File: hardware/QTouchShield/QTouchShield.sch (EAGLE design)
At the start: 114 parts, among them IC1 AT32UC3C0512CJEDEC-MS-026, U1 ARDUINO-MEGALITE

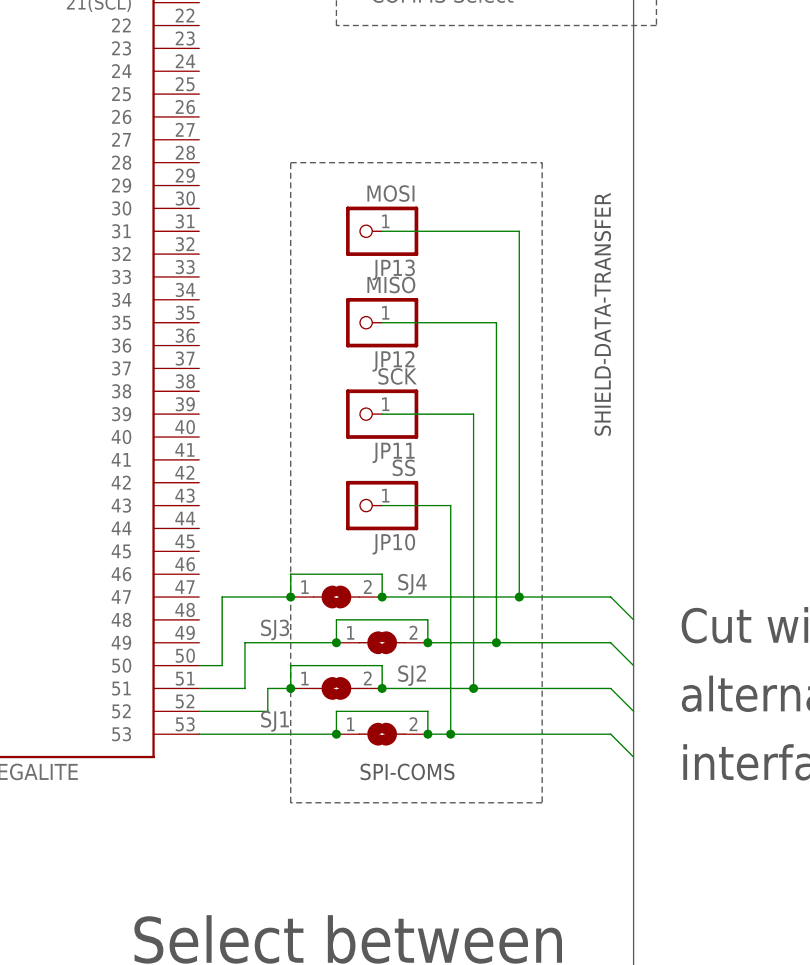
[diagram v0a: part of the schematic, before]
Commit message: Swapped MISO/MOSI connection to Arduino - wrong way round.
The MISO/MOSI lines from the UC3C to the Arduino were swapped.
Fixed in the schematic and board.
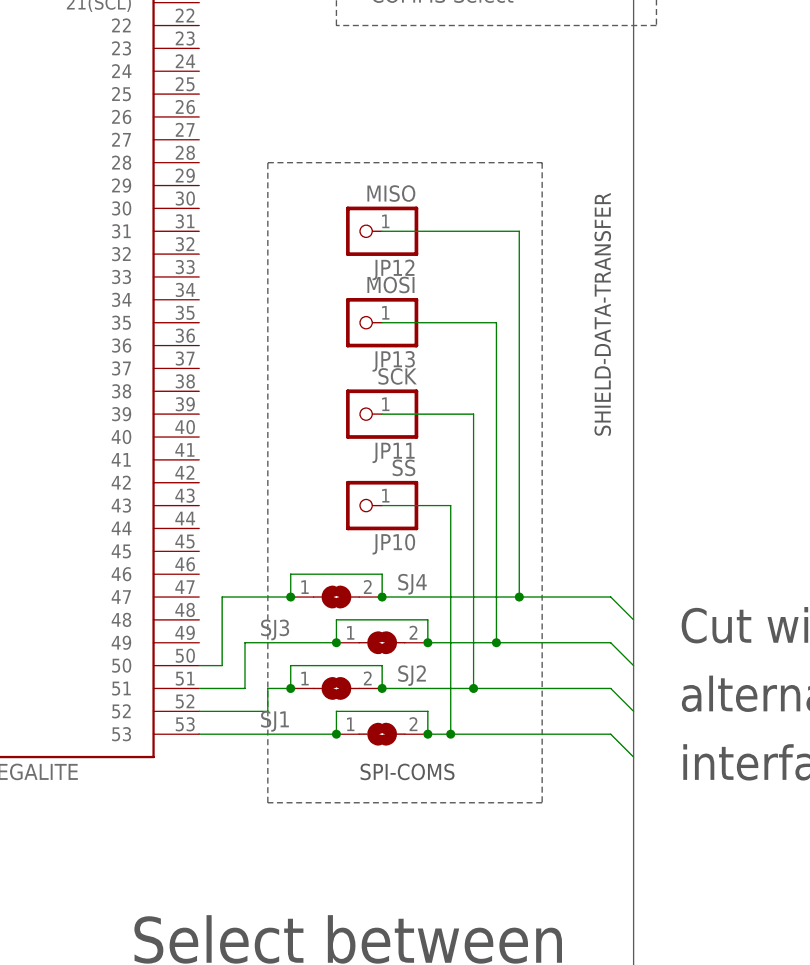
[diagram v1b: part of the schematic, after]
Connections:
- net SDT-SPI0-MISO: now also SJ4.1, SJ4.2, U1.50; no longer SJ3.1, SJ3.2, U1.51
- net SDT-SPI0-MOSI: now also SJ3.1, SJ3.2, U1.51; no longer SJ4.1, SJ4.2, U1.50
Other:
- moved on the sheet: JP12, JP13
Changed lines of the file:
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@@
 <setting verticaltext="up"/>
 </settings>
-<grid distance="0.1" unitdist="mm" unit="mm" style="lines" multiple="1" display="yes" altdistance="0.01" altunitdist="inch" altunit="inch"/>
+<grid distance="0.1" unitdist="inch" unit="inch" style="lines" multiple="1" display="no" altdistance="0.01" altunitdist="inch" altunit="inch"/>
 <layers>
 <layer number="1" name="Top" color="4" fill="1" visible="no" active="no"/>
@@
 <layer number="91" name="Nets" color="2" fill="1" visible="yes" active="yes"/>
 <layer number="92" name="Busses" color="1" fill="1" visible="yes" active="yes"/>
-<layer number="93" name="Pins" color="2" fill="1" visible="yes" active="yes"/>
+<layer number="93" name="Pins" color="2" fill="1" visible="no" active="yes"/>
 <layer number="94" name="Symbols" color="4" fill="1" visible="yes" active="yes"/>
 <layer number="95" name="Names" color="7" fill="1" visible="yes" active="yes"/>
@@
 <wire x1="-2.54" y1="-109.22" x2="-96.52" y2="-109.22" width="0.1524" layer="97" style="shortdash"/>
 <wire x1="-96.52" y1="-109.22" x2="-96.52" y2="-106.68" width="0.1524" layer="97" style="shortdash"/>
-<wire x1="256.54" y1="-45.72" x2="256.54" y2="25.4" width="0.1524" layer="97" style="shortdash"/>
-<wire x1="256.54" y1="25.4" x2="284.48" y2="25.4" width="0.1524" layer="97" style="shortdash"/>
+<wire x1="254" y1="-45.72" x2="254" y2="25.4" width="0.1524" layer="97" style="shortdash"/>
+<wire x1="254" y1="25.4" x2="284.48" y2="25.4" width="0.1524" layer="97" style="shortdash"/>
 <wire x1="284.48" y1="25.4" x2="284.48" y2="-45.72" width="0.1524" layer="97" style="shortdash"/>
-<wire x1="284.48" y1="-45.72" x2="256.54" y2="-45.72" width="0.1524" layer="97" style="shortdash"/>
+<wire x1="284.48" y1="-45.72" x2="254" y2="-45.72" width="0.1524" layer="97" style="shortdash"/>
 <text x="170.18" y="25.4" size="1.778" layer="97" rot="R90">Use to link AT32UC3C</text>
 <text x="172.72" y="25.4" size="1.778" layer="97" rot="R90">RESET_N to</text>
@@
 <instance part="JP10" gate="G$1" x="264.16" y="-12.7" rot="R180"/>
 <instance part="JP11" gate="G$1" x="264.16" y="-2.54" rot="R180"/>
-<instance part="JP12" gate="G$1" x="264.16" y="7.62" rot="R180"/>
-<instance part="JP13" gate="G$1" x="264.16" y="17.78" rot="R180"/>
+<instance part="JP12" gate="G$1" x="264.16" y="17.78" rot="R180"/>
+<instance part="JP13" gate="G$1" x="264.16" y="7.62" rot="R180"/>
 <instance part="JP14" gate="G$1" x="228.6" y="73.66" rot="R180"/>
 <instance part="JP15" gate="G$1" x="185.42" y="-7.62" rot="R180"/>
@@
 </segment>
 <segment>
-<wire x1="294.64" y1="-25.4" x2="292.1" y2="-22.86" width="0.1524" layer="91"/>
-<wire x1="292.1" y1="-22.86" x2="281.94" y2="-22.86" width="0.1524" layer="91"/>
-<pinref part="SJ4" gate="1" pin="2"/>
+<wire x1="294.64" y1="-30.48" x2="292.1" y2="-27.94" width="0.1524" layer="91"/>
+<pinref part="SJ3" gate="1" pin="2"/>
+<wire x1="279.4" y1="-27.94" x2="271.78" y2="-27.94" width="0.1524" layer="91"/>
+<pinref part="SJ3" gate="1" pin="1"/>
+<wire x1="261.62" y1="-27.94" x2="261.62" y2="-25.4" width="0.1524" layer="91"/>
+<wire x1="261.62" y1="-25.4" x2="271.78" y2="-25.4" width="0.1524" layer="91"/>
+<wire x1="271.78" y1="-25.4" x2="271.78" y2="-27.94" width="0.1524" layer="91"/>
+<junction x="271.78" y="-27.94"/>
+<wire x1="292.1" y1="-27.94" x2="279.4" y2="-27.94" width="0.1524" layer="91"/>
+<pinref part="U1" gate="G$1" pin="51"/>
+<wire x1="251.46" y1="-27.94" x2="251.46" y2="-33.02" width="0.1524" layer="91"/>
+<wire x1="251.46" y1="-33.02" x2="246.38" y2="-33.02" width="0.1524" layer="91"/>
+<wire x1="261.62" y1="-27.94" x2="251.46" y2="-27.94" width="0.1524" layer="91"/>
+<junction x="261.62" y="-27.94"/>
 <pinref part="JP13" gate="G$1" pin="1"/>
-<wire x1="281.94" y1="-22.86" x2="266.7" y2="-22.86" width="0.1524" layer="91"/>
-<wire x1="281.94" y1="-22.86" x2="281.94" y2="17.78" width="0.1524" layer="91"/>
-<wire x1="281.94" y1="17.78" x2="266.7" y2="17.78" width="0.1524" layer="91"/>
-<junction x="281.94" y="-22.86"/>
-<wire x1="256.54" y1="-22.86" x2="248.92" y2="-22.86" width="0.1524" layer="91"/>
-<wire x1="248.92" y1="-22.86" x2="248.92" y2="-30.48" width="0.1524" layer="91"/>
-<pinref part="U1" gate="G$1" pin="50"/>
-<wire x1="248.92" y1="-30.48" x2="246.38" y2="-30.48" width="0.1524" layer="91"/>
-<pinref part="SJ4" gate="1" pin="1"/>
-<wire x1="256.54" y1="-22.86" x2="256.54" y2="-20.32" width="0.1524" layer="91"/>
-<junction x="256.54" y="-22.86"/>
-<wire x1="256.54" y1="-20.32" x2="266.7" y2="-20.32" width="0.1524" layer="91"/>
-<wire x1="266.7" y1="-20.32" x2="266.7" y2="-22.86" width="0.1524" layer="91"/>
-<junction x="266.7" y="-22.86"/>
+<wire x1="266.7" y1="7.62" x2="279.4" y2="7.62" width="0.1524" layer="91"/>
+<wire x1="279.4" y1="7.62" x2="279.4" y2="-27.94" width="0.1524" layer="91"/>
+<junction x="279.4" y="-27.94"/>
 </segment>
 </net>
@@
 </segment>
 <segment>
-<wire x1="294.64" y1="-30.48" x2="292.1" y2="-27.94" width="0.1524" layer="91"/>
-<wire x1="292.1" y1="-27.94" x2="279.4" y2="-27.94" width="0.1524" layer="91"/>
-<pinref part="SJ3" gate="1" pin="2"/>
-<wire x1="279.4" y1="-27.94" x2="271.78" y2="-27.94" width="0.1524" layer="91"/>
-<wire x1="279.4" y1="-27.94" x2="279.4" y2="7.62" width="0.1524" layer="91"/>
-<wire x1="279.4" y1="7.62" x2="266.7" y2="7.62" width="0.1524" layer="91"/>
-<junction x="279.4" y="-27.94"/>
+<wire x1="294.64" y1="-25.4" x2="292.1" y2="-22.86" width="0.1524" layer="91"/>
+<pinref part="SJ4" gate="1" pin="2"/>
+<wire x1="281.94" y1="-22.86" x2="266.7" y2="-22.86" width="0.1524" layer="91"/>
+<pinref part="SJ4" gate="1" pin="1"/>
+<wire x1="256.54" y1="-22.86" x2="256.54" y2="-20.32" width="0.1524" layer="91"/>
+<wire x1="256.54" y1="-20.32" x2="266.7" y2="-20.32" width="0.1524" layer="91"/>
+<wire x1="266.7" y1="-20.32" x2="266.7" y2="-22.86" width="0.1524" layer="91"/>
+<junction x="266.7" y="-22.86"/>
+<wire x1="292.1" y1="-22.86" x2="281.94" y2="-22.86" width="0.1524" layer="91"/>
+<pinref part="U1" gate="G$1" pin="50"/>
+<wire x1="248.92" y1="-22.86" x2="248.92" y2="-30.48" width="0.1524" layer="91"/>
+<wire x1="248.92" y1="-30.48" x2="246.38" y2="-30.48" width="0.1524" layer="91"/>
+<wire x1="256.54" y1="-22.86" x2="248.92" y2="-22.86" width="0.1524" layer="91"/>
+<junction x="256.54" y="-22.86"/>
 <pinref part="JP12" gate="G$1" pin="1"/>
-<wire x1="261.62" y1="-27.94" x2="251.46" y2="-27.94" width="0.1524" layer="91"/>
-<wire x1="251.46" y1="-27.94" x2="251.46" y2="-33.02" width="0.1524" layer="91"/>
-<pinref part="U1" gate="G$1" pin="51"/>
-<wire x1="251.46" y1="-33.02" x2="246.38" y2="-33.02" width="0.1524" layer="91"/>
-<pinref part="SJ3" gate="1" pin="1"/>
-<wire x1="261.62" y1="-27.94" x2="261.62" y2="-25.4" width="0.1524" layer="91"/>
-<junction x="261.62" y="-27.94"/>
-<wire x1="261.62" y1="-25.4" x2="271.78" y2="-25.4" width="0.1524" layer="91"/>
-<wire x1="271.78" y1="-25.4" x2="271.78" y2="-27.94" width="0.1524" layer="91"/>
-<junction x="271.78" y="-27.94"/>
+<wire x1="266.7" y1="17.78" x2="281.94" y2="17.78" width="0.1524" layer="91"/>
+<wire x1="281.94" y1="17.78" x2="281.94" y2="-22.86" width="0.1524" layer="91"/>
+<junction x="281.94" y="-22.86"/>
 </segment>
 </net>

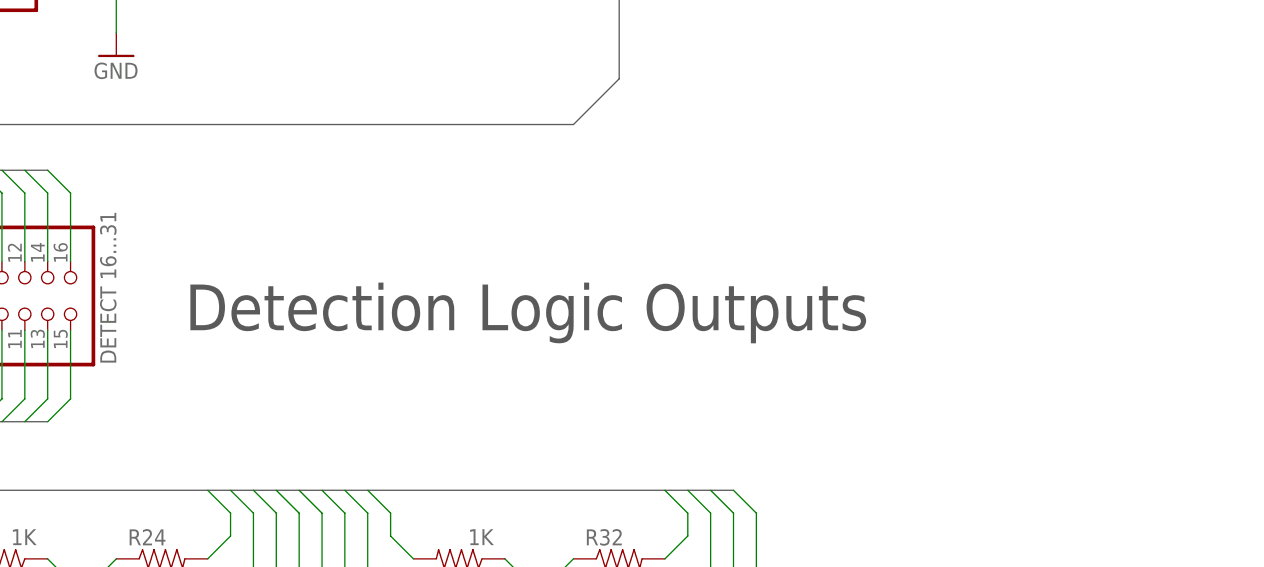
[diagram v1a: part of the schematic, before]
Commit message: Added comment regarding detect pins on schematic.
Noted that detect pins output "channel" detections, not "sensor"
detections, as defined in the QTouch library.
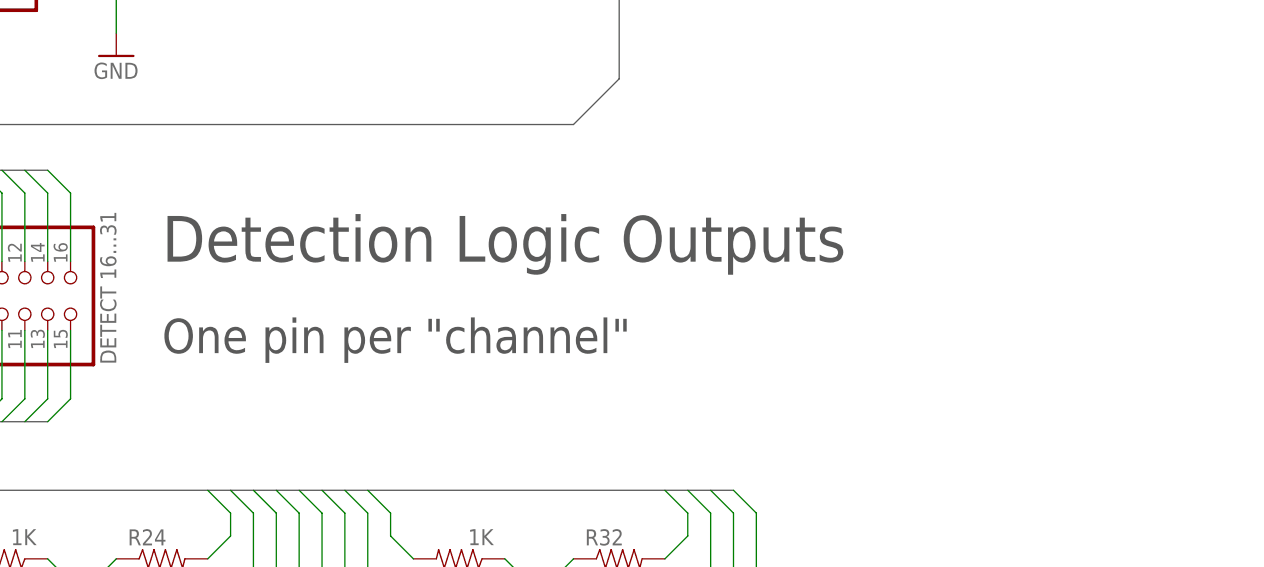
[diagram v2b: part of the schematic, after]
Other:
- note added: "One pin per "channel""
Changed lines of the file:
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@@
 <text x="-66.04" y="88.9" size="1.778" layer="97">Keep close to pins 34 &amp; 35</text>
 <text x="175.26" y="-248.92" size="5.08" layer="97">Sensor Headers</text>
-<text x="246.38" y="-144.78" size="5.08" layer="97">Detection Logic Outputs</text>
+<text x="243.84" y="-137.16" size="5.08" layer="97">Detection Logic Outputs</text>
 <text x="299.72" y="-27.94" size="3.81" layer="97">Cut wires to use</text>
 <text x="299.72" y="-35.56" size="3.81" layer="97">alternative SPI</text>
@@
 <rectangle x1="-77.75" y1="-158.05" x2="-75.95" y2="-157.95" layer="200"/>
 <wire x1="-2.54" y1="-151.48" x2="-96.52" y2="-151.48" width="0.1524" layer="97" style="shortdash"/>
+<text x="243.84" y="-147.32" size="3.81" layer="97">One pin per "channel"</text>
 </plain>
 <instances>
